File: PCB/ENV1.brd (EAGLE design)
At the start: 100 x 80 mm, 46 parts, among them IC1 78L05, IC2 4066D, IC3 MCP6002, IC4 TL072D, SW1 TL2285, T1 BC847

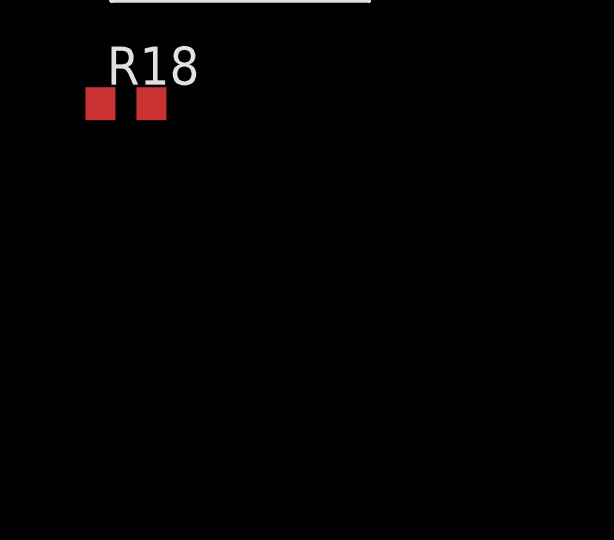
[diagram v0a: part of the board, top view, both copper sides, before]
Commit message: Value adjustments for timing capacitors. Added forgotten diode in -12V supply.
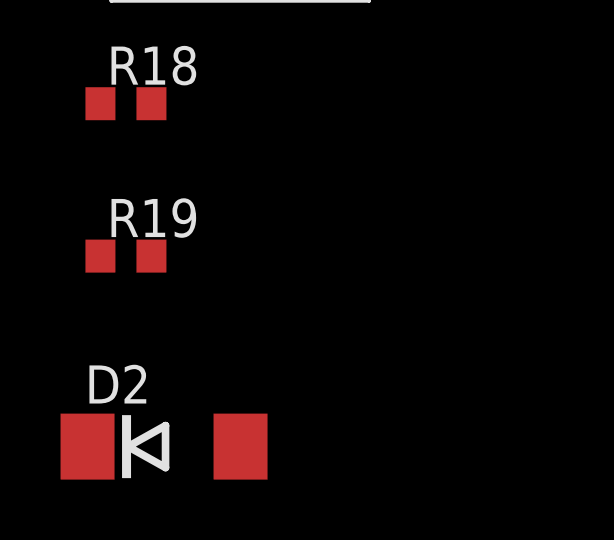
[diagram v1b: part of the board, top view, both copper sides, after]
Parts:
- added D2: 1N4004 equiv, diode:DO214AA
- added R19: 100, rcl:R0603
- C1, C2, C6: value 10u -> 10u 16V
- C10, C7: value 470n -> 1u
- C11, C12: value 4,7u -> 10u
- JP1: value (none) -> EURORACK PSU
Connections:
- new net N$14: D2.C, JP1.10, JP1.9
- new net N$18: R19.2, SW1.1
- net -12V: now also D2.A; no longer JP1.10, JP1.9
- net GND: now also R19.1
- net N$1: now also SW1.2; no longer SW1.3
- net N$16: now also SW1.3; no longer SW1.2
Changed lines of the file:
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@@
 </autorouter>
 <elements>
-<element name="C10" library="rcl" package="C1206K" value="470n" x="-43.18" y="40.64"/>
+<element name="C10" library="rcl" package="C1206K" value="1u" x="-43.18" y="40.64"/>
 <element name="C5" library="rcl" package="C0603K" value="100n" x="-35.56" y="52.07"/>
-<element name="C7" library="rcl" package="C0603K" value="470n" x="-40.64" y="52.07"/>
+<element name="C7" library="rcl" package="C0603K" value="1u" x="-40.64" y="52.07"/>
 <element name="C8" library="rcl" package="C0603K" value="100n" x="-45.72" y="52.07"/>
 <element name="C9" library="rcl" package="C0603K" value="100n" x="-50.8" y="52.07"/>
@@
 <element name="IC2" library="40xx" package="SO14" value="4066D" x="-17.78" y="33.02"/>
 <element name="IC3" library="linear" package="SO08" value="MCP6002" x="-30.48" y="19.05"/>
-<element name="JP1" library="pinhead" package="2X05" value="" x="-31.75" y="31.75"/>
+<element name="JP1" library="pinhead" package="2X05" value="EURORACK PSU" x="-31.75" y="31.75"/>
 <element name="LED1" library="led" package="LED3MM" value="" x="-35.56" y="46.99"/>
 <element name="LED2" library="led" package="LED3MM" value="" x="-45.72" y="46.99"/>
@@
 <element name="T1" library="transistor" package="SOT23" value="BC847" x="-62.23" y="-8.89"/>
 <element name="R10" library="rcl" package="R0603" value="10k" x="-62.23" y="-15.24"/>
-<element name="C6" library="rcl" package="C1206K" value="10u" x="-62.23" y="-20.32"/>
-<element name="C1" library="rcl" package="C1206K" value="10u" x="-62.23" y="-25.4"/>
-<element name="C2" library="rcl" package="C1206K" value="10u" x="-62.23" y="-30.48"/>
+<element name="C6" library="rcl" package="C1206K" value="10u 16V" x="-62.23" y="-20.32"/>
+<element name="C1" library="rcl" package="C1206K" value="10u 16V" x="-62.23" y="-25.4"/>
+<element name="C2" library="rcl" package="C1206K" value="10u 16V" x="-62.23" y="-30.48"/>
 <element name="IC4" library="linear" package="SO08" value="TL072D" x="-69.85" y="-29.21"/>
 <element name="R11" library="rcl" package="R0603" value="60k" x="-72.39" y="-35.56"/>
@@
 <element name="C4" library="rcl" package="C0603K" value="100n" x="-83.82" y="-55.88"/>
 <element name="SW1" library="lb_devs" package="TL2285_PCB" value="TL2285" x="-81.28" y="-62.23"/>
-<element name="C11" library="rcl" package="C1206K" value="4,7u" x="-83.82" y="-69.85"/>
-<element name="C12" library="rcl" package="C0603K" value="4,7u" x="-83.82" y="-74.93"/>
+<element name="C11" library="rcl" package="C1206K" value="10u" x="-83.82" y="-69.85"/>
+<element name="C12" library="rcl" package="C0603K" value="10u" x="-83.82" y="-74.93"/>
 <element name="R14" library="rcl" package="R0603" value="60k" x="-83.82" y="-80.01"/>
 <element name="R15" library="rcl" package="R0603" value="100k" x="-83.82" y="-85.09"/>
@@
 <element name="R17" library="pot-alps" package="ALPS_POT_VERTICAL" value="100k" x="-104.14" y="-86.36"/>
 <element name="R18" library="rcl" package="R0603" value="100" x="-107.95" y="-95.25"/>
+<element name="R19" library="rcl" package="R0603" value="100" x="-107.95" y="-100.33"/>
+<element name="D2" library="diode" package="DO214AA" value="1N4004 equiv" x="-106.68" y="-106.68"/>
 </elements>
 <signals>
@@
 <contactref element="R15" pad="2"/>
 <contactref element="R17" pad="P$3"/>
+<contactref element="R19" pad="1"/>
+<wire x1="-91.44" y1="-90.32" x2="-108.8" y2="-100.33" width="0" layer="19" extent="1-1"/>
 <wire x1="-82.97" y1="-85.09" x2="-91.44" y2="-90.32" width="0" layer="19" extent="1-1"/>
 <wire x1="-82.945" y1="-74.93" x2="-82.97" y2="-85.09" width="0" layer="19" extent="1-1"/>
@@
 </signal>
 <signal name="-12V">
-<contactref element="JP1" pad="9"/>
-<contactref element="JP1" pad="10"/>
 <contactref element="C2" pad="2"/>
 <contactref element="C4" pad="2"/>
 <contactref element="IC4" pad="4"/>
+<contactref element="D2" pad="A"/>
+<wire x1="-82.945" y1="-55.88" x2="-104.13" y2="-106.68" width="0" layer="19" extent="1-1"/>
 <wire x1="-67.945" y1="-31.81" x2="-82.945" y2="-55.88" width="0" layer="19" extent="1-1"/>
 <wire x1="-60.73" y1="-30.48" x2="-67.945" y2="-31.81" width="0" layer="19" extent="1-1"/>
-<wire x1="-26.67" y1="30.48" x2="-60.73" y2="-30.48" width="0" layer="19" extent="1-1"/>
-<wire x1="-26.67" y1="33.02" x2="-26.67" y2="30.48" width="0" layer="19" extent="1-1"/>
 </signal>
 <signal name="N$1">
@@
 <contactref element="C10" pad="1"/>
 <contactref element="IC4" pad="5"/>
-<contactref element="SW1" pad="3"/>
 <contactref element="R18" pad="2"/>
-<wire x1="-78.78" y1="-65.23" x2="-107.1" y2="-95.25" width="0" layer="19" extent="1-1"/>
-<wire x1="-67.945" y1="-26.61" x2="-78.78" y2="-65.23" width="0" layer="19" extent="1-1"/>
+<contactref element="SW1" pad="2"/>
+<wire x1="-81.28" y1="-65.23" x2="-107.1" y2="-95.25" width="0" layer="19" extent="1-1"/>
+<wire x1="-67.945" y1="-26.61" x2="-81.28" y2="-65.23" width="0" layer="19" extent="1-1"/>
 <wire x1="-29.845" y1="16.45" x2="-67.945" y2="-26.61" width="0" layer="19" extent="1-1"/>
 <wire x1="-44.68" y1="40.64" x2="-29.845" y2="16.45" width="0" layer="19" extent="1-1"/>
@@
 </signal>
 <signal name="N$16">
-<contactref element="SW1" pad="2"/>
 <contactref element="C12" pad="1"/>
 <contactref element="C11" pad="1"/>
+<contactref element="SW1" pad="3"/>
 <wire x1="-85.32" y1="-69.85" x2="-84.695" y2="-74.93" width="0" layer="19" extent="1-1"/>
-<wire x1="-81.28" y1="-65.23" x2="-85.32" y2="-69.85" width="0" layer="19" extent="1-1"/>
+<wire x1="-78.78" y1="-65.23" x2="-85.32" y2="-69.85" width="0" layer="19" extent="1-1"/>
 </signal>
 <signal name="N$19">
@@
 <wire x1="-15.24" y1="36.0934" x2="-16.51" y2="36.0934" width="0" layer="19" extent="1-1"/>
 </signal>
+<signal name="N$18">
+<contactref element="SW1" pad="1"/>
+<contactref element="R19" pad="2"/>
+<wire x1="-83.78" y1="-65.23" x2="-107.1" y2="-100.33" width="0" layer="19" extent="1-1"/>
+</signal>
+<signal name="N$14">
+<contactref element="JP1" pad="10"/>
+<contactref element="JP1" pad="9"/>
+<contactref element="D2" pad="C"/>
+<wire x1="-26.67" y1="30.48" x2="-109.23" y2="-106.68" width="0" layer="19" extent="1-1"/>
+<wire x1="-26.67" y1="33.02" x2="-26.67" y2="30.48" width="0" layer="19" extent="1-1"/>
+</signal>
 </signals>

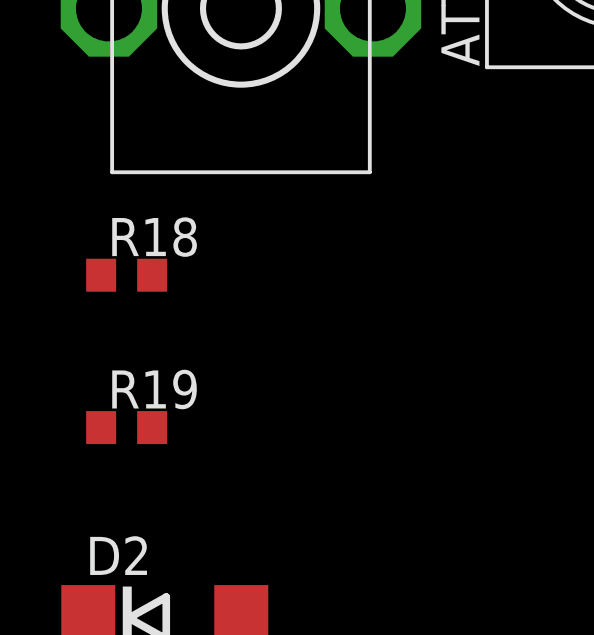
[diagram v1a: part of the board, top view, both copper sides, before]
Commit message: Added handling of 74HC4017 counter chip that manages the UI LEDs. Added same chip to schematic.
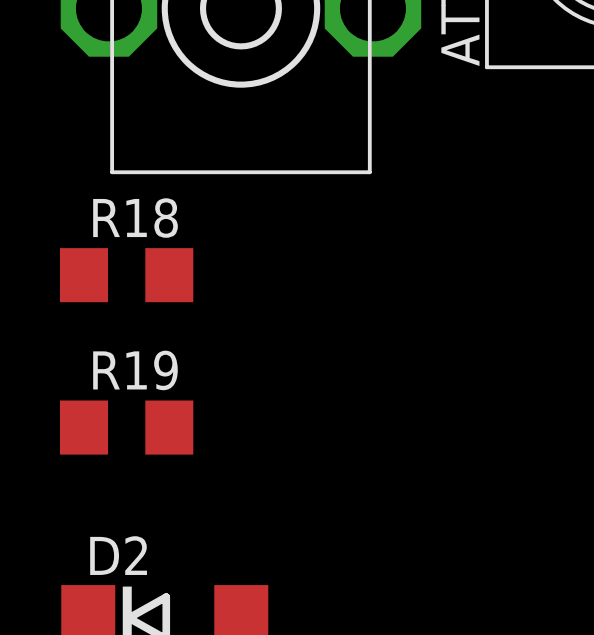
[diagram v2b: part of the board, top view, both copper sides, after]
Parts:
- R18, R19: device rcl:R0603 -> rcl:R1206
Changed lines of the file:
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@@
 <element name="ATT_OUT" library="thonkiconn" package="WQP-PJ301M-12_JACK" value="WQP-PJ301M-12_JACK" x="-91.44" y="-83.82"/>
 <element name="R17" library="pot-alps" package="ALPS_POT_VERTICAL" value="100k" x="-104.14" y="-86.36"/>
-<element name="R18" library="rcl" package="R0603" value="100" x="-107.95" y="-95.25"/>
-<element name="R19" library="rcl" package="R0603" value="100" x="-107.95" y="-100.33"/>
+<element name="R18" library="rcl" package="R1206" value="100" x="-107.95" y="-95.25"/>
+<element name="R19" library="rcl" package="R1206" value="100" x="-107.95" y="-100.33"/>
 <element name="D2" library="diode" package="DO214AA" value="1N4004 equiv" x="-106.68" y="-106.68"/>
 </elements>
@@
 <contactref element="R17" pad="P$3"/>
 <contactref element="R19" pad="1"/>
-<wire x1="-91.44" y1="-90.32" x2="-108.8" y2="-100.33" width="0" layer="19" extent="1-1"/>
+<wire x1="-91.44" y1="-90.32" x2="-109.372" y2="-100.33" width="0" layer="19" extent="1-1"/>
 <wire x1="-82.97" y1="-85.09" x2="-91.44" y2="-90.32" width="0" layer="19" extent="1-1"/>
 <wire x1="-82.945" y1="-74.93" x2="-82.97" y2="-85.09" width="0" layer="19" extent="1-1"/>
@@
 <contactref element="R18" pad="2"/>
 <contactref element="SW1" pad="2"/>
-<wire x1="-81.28" y1="-65.23" x2="-107.1" y2="-95.25" width="0" layer="19" extent="1-1"/>
+<wire x1="-81.28" y1="-65.23" x2="-106.528" y2="-95.25" width="0" layer="19" extent="1-1"/>
 <wire x1="-67.945" y1="-26.61" x2="-81.28" y2="-65.23" width="0" layer="19" extent="1-1"/>
 <wire x1="-29.845" y1="16.45" x2="-67.945" y2="-26.61" width="0" layer="19" extent="1-1"/>
@@
 <contactref element="IC2" pad="2"/>
 <contactref element="R18" pad="1"/>
-<wire x1="-20.32" y1="29.9466" x2="-108.8" y2="-95.25" width="0" layer="19" extent="1-1"/>
+<wire x1="-20.32" y1="29.9466" x2="-109.372" y2="-95.25" width="0" layer="19" extent="1-1"/>
 <wire x1="-19.05" y1="29.9466" x2="-20.32" y2="29.9466" width="0" layer="19" extent="1-1"/>
 <wire x1="-16.51" y1="36.0934" x2="-19.05" y2="29.9466" width="0" layer="19" extent="1-1"/>
@@
 <contactref element="SW1" pad="1"/>
 <contactref element="R19" pad="2"/>
-<wire x1="-83.78" y1="-65.23" x2="-107.1" y2="-100.33" width="0" layer="19" extent="1-1"/>
+<wire x1="-83.78" y1="-65.23" x2="-106.528" y2="-100.33" width="0" layer="19" extent="1-1"/>
 </signal>
 <signal name="N$14">
